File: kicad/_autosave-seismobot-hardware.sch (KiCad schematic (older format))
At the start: 98 parts, among them J1 Screw_Terminal_01x02, J2 Raspberry_Pi_2_3, U1 OPA2156xD, U10 AP7340, U2 OPA2156xD, U3 ref-6, U4 ref-8, U5 LTC6011, U6 OPA2156xD, U7 OPA2156xD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

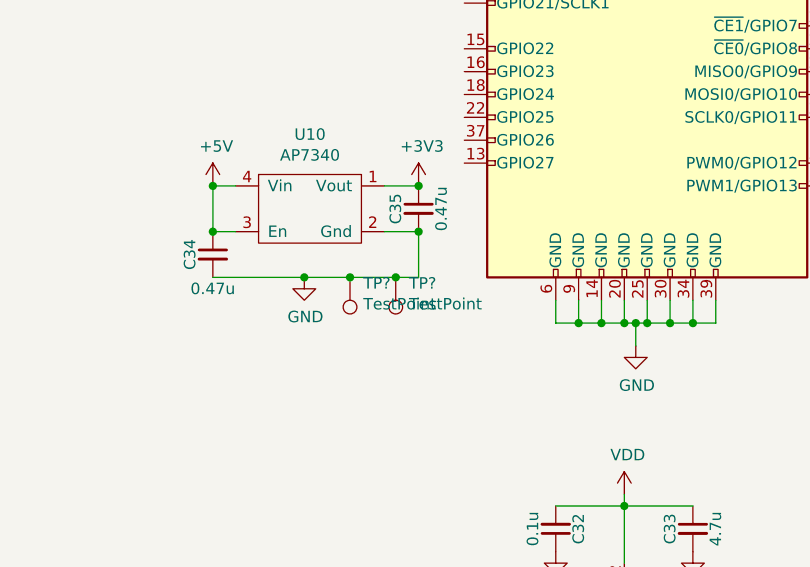
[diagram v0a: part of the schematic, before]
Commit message: add 3v3 regulator, more routing
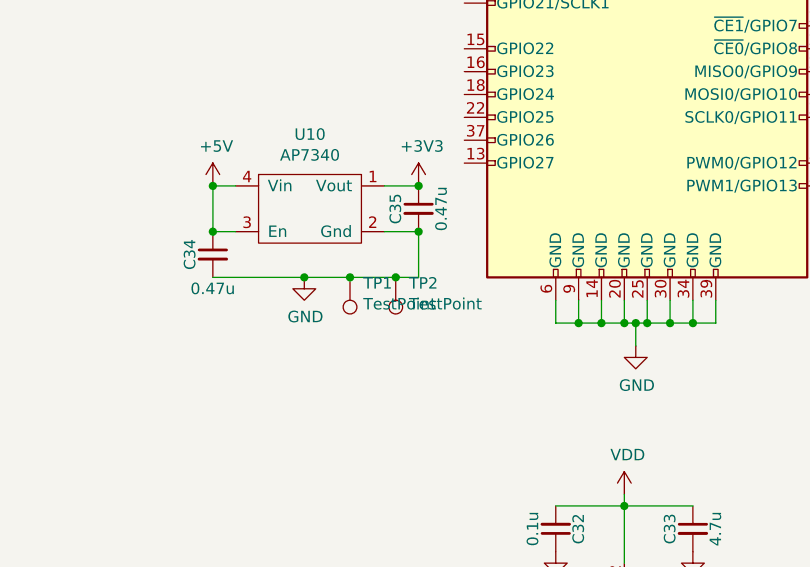
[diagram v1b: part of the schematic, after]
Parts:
- gave numbers to parts that had none: 2
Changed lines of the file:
@@
 Connection ~ 8950 3350
 $Comp
-L Connector:TestPoint TP?
+L Connector:TestPoint TP2
 U 1 1 6146A6B1
 P 8850 3550
-F 0 "TP?" H 8792 3576 50  0000 R CNN
+F 0 "TP2" H 8792 3576 50  0000 R CNN
 F 1 "TestPoint" H 8792 3667 50  0000 R CNN
 F 2 "Connector_PinHeader_2.54mm:PinHeader_1x01_P2.54mm_Vertical" H 9050 3550 50  0001 C CNN
@@
 $EndComp
 $Comp
-L Connector:TestPoint TP?
+L Connector:TestPoint TP1
 U 1 1 6146B4AA
 P 8650 3550
-F 0 "TP?" H 8592 3576 50  0000 R CNN
+F 0 "TP1" H 8592 3576 50  0000 R CNN
 F 1 "TestPoint" H 8592 3667 50  0000 R CNN
 F 2 "Connector_PinHeader_2.54mm:PinHeader_1x01_P2.54mm_Vertical" H 8850 3550 50  0001 C CNN
